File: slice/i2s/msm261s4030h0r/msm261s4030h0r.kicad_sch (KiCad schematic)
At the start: 3 parts, among them U1 MSM261S4030H0R

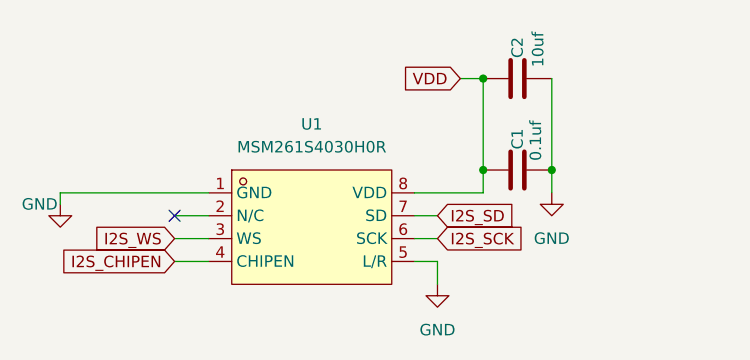
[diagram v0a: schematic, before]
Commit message: Update position of capacitor in `i2s/msm261s4030h0r`
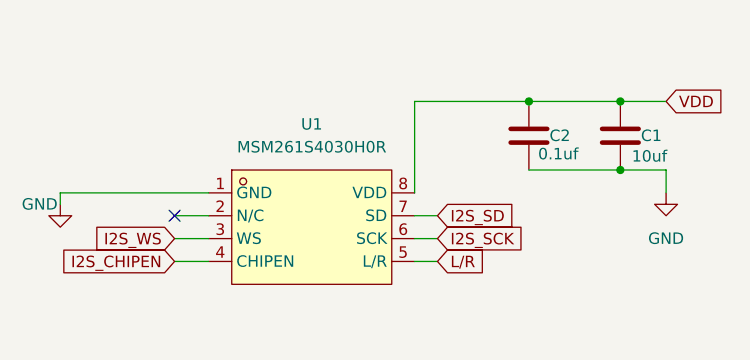
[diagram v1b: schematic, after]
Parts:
- C1: value 0.1uf -> 10uf
- C2: value 10uf -> 0.1uf
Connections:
- net GND: no longer U1.5 (L/R)
- new net L/R: U1.5 (L/R)
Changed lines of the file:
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@@
 	(paper "A4")
 	(junction
-		(at 175.26 92.71)
+		(at 182.88 85.09)
 		(diameter 0)
 		(color 0 0 0 0)
 	)
 	(junction
-		(at 167.64 82.55)
+		(at 172.72 85.09)
 		(diameter 0)
 		(color 0 0 0 0)
 	)
 	(junction
-		(at 167.64 92.71)
+		(at 182.88 92.71)
 		(diameter 0)
 		(color 0 0 0 0)
@@
 	(wire
 		(pts
-			(xy 167.64 92.71) (xy 167.64 95.25)
-		)
-		(stroke
-			(width 0)
-			(type default)
-		)
-	)
-	(wire
-		(pts
-			(xy 162.56 102.87) (xy 162.56 105.41)
-		)
-		(stroke
-			(width 0)
-			(type default)
-		)
-	)
-	(wire
-		(pts
-			(xy 175.26 92.71) (xy 175.26 95.25)
+			(xy 187.96 92.71) (xy 187.96 95.25)
+		)
+		(stroke
+			(width 0)
+			(type default)
+		)
+	)
+	(wire
+		(pts
+			(xy 172.72 85.09) (xy 182.88 85.09)
 		)
 		(stroke
@@
 	(wire
 		(pts
-			(xy 167.64 95.25) (xy 160.02 95.25)
+			(xy 172.72 92.71) (xy 182.88 92.71)
 		)
 		(stroke
@@
 	(wire
 		(pts
-			(xy 165.1 82.55) (xy 167.64 82.55)
-		)
-		(stroke
-			(width 0)
-			(type default)
-		)
-	)
-	(wire
-		(pts
-			(xy 167.64 82.55) (xy 167.64 92.71)
+			(xy 187.96 92.71) (xy 182.88 92.71)
 		)
 		(stroke
@@
 	(wire
 		(pts
+			(xy 160.02 85.09) (xy 160.02 95.25)
+		)
+		(stroke
+			(width 0)
+			(type default)
+		)
+	)
+	(wire
+		(pts
 			(xy 133.35 100.33) (xy 137.16 100.33)
 		)
@@
 	(wire
 		(pts
-			(xy 175.26 92.71) (xy 175.26 82.55)
+			(xy 160.02 85.09) (xy 172.72 85.09)
+		)
+		(stroke
+			(width 0)
+			(type default)
+		)
+	)
+	(wire
+		(pts
+			(xy 182.88 85.09) (xy 187.96 85.09)
 		)
 		(stroke
@@
 		)
 	)
+	(global_label "L{slash}R"
+		(shape input)
+		(at 162.56 102.87 0)
+		(fields_autoplaced yes)
+		(effects
+			(font
+				(size 1.27 1.27)
+			)
+			(justify left)
+		)
+		(property "Intersheetrefs" "${INTERSHEET_REFS}"
+			(at 169.1738 102.87 0)
+			(effects
+				(font
+					(size 1.27 1.27)
+				)
+				(justify left)
+				(hide yes)
+			)
+		)
+	)
 	(global_label "I2S_CHIPEN"
 		(shape input)
@@
 	(global_label "VDD"
 		(shape input)
-		(at 165.1 82.55 180)
+		(at 187.96 85.09 0)
 		(fields_autoplaced yes)
 		(effects
@@
 				(size 1.27 1.27)
 			)
-			(justify right)
+			(justify left)
 		)
 		(property "Intersheetrefs" "${INTERSHEET_REFS}"
-			(at 158.4862 82.55 0)
-			(effects
-				(font
-					(size 1.27 1.27)
-				)
-				(justify right)
+			(at 194.5738 85.09 0)
+			(effects
+				(font
+					(size 1.27 1.27)
+				)
+				(justify left)
 				(hide yes)
 			)
@@
 	(symbol
 		(lib_id "power:GND")
-		(at 175.26 95.25 0)
+		(at 187.96 95.25 0)
 		(unit 1)
 		(exclude_from_sim no)
@@
 		(dnp no)
 		(fields_autoplaced yes)
-		(property "Reference" "#PWR03"
-			(at 175.26 101.6 0)
+		(property "Reference" "#PWR01"
+			(at 187.96 101.6 0)
 			(effects
 				(font
@@
 		)
 		(property "Value" "GND"
-			(at 175.26 100.33 0)
+			(at 187.96 100.33 0)
 			(effects
 				(font
@@
 		)
 		(property "Footprint" ""
-			(at 175.26 95.25 0)
+			(at 187.96 95.25 0)
 			(effects
 				(font
@@
 		)
 		(property "Datasheet" ""
-			(at 175.26 95.25 0)
+			(at 187.96 95.25 0)
 			(effects
 				(font
@@
 		)
 		(property "Description" "Power symbol creates a global label with name \"GND\" , ground"
-			(at 175.26 95.25 0)
+			(at 187.96 95.25 0)
 			(effects
 				(font
@@
 		(instances
 			(project "msm261s4030h0r"
-				(path "/3ead2bbc-d546-4367-b51b-7ed83f32863a"
-					(reference "#PWR03")
-					(unit 1)
-				)
-			)
-		)
-	)
-	(symbol
-		(lib_id "Device:C")
-		(at 171.45 92.71 90)
-		(unit 1)
-		(exclude_from_sim no)
-		(in_bom yes)
-		(on_board yes)
-		(dnp no)
-		(property "Reference" "C1"
-			(at 171.45 90.424 0)
-			(do_not_autoplace yes)
-			(effects
-				(font
-					(size 1.27 1.27)
-				)
-				(justify left)
-			)
-		)
-		(property "Value" "0.1uf"
-			(at 173.482 91.694 0)
-			(do_not_autoplace yes)
-			(effects
-				(font
-					(size 1.27 1.27)
-				)
-				(justify left)
-			)
-		)
-		(property "Footprint" ""
-			(at 175.26 91.7448 0)
-			(effects
-				(font
-					(size 1.27 1.27)
-				)
-				(hide yes)
-			)
-		)
-		(property "Datasheet" "~"
-			(at 171.45 92.71 0)
-			(effects
-				(font
-					(size 1.27 1.27)
-				)
-				(hide yes)
-			)
-		)
-		(property "Description" "Unpolarized capacitor"
-			(at 171.45 92.71 0)
-			(effects
-				(font
-					(size 1.27 1.27)
-				)
-				(hide yes)
-			)
-		)
-		(pin "1"
-		)
-		(pin "2"
-		)
-		(instances
-			(project "msm261s4030h0r"
-				(path "/3ead2bbc-d546-4367-b51b-7ed83f32863a"
-					(reference "C1")
-					(unit 1)
-				)
-			)
-		)
-	)
-	(symbol
-		(lib_id "power:GND")
-		(at 162.56 105.41 0)
-		(unit 1)
-		(exclude_from_sim no)
-		(in_bom yes)
-		(on_board yes)
-		(dnp no)
-		(fields_autoplaced yes)
-		(property "Reference" "#PWR01"
-			(at 162.56 111.76 0)
-			(effects
-				(font
-					(size 1.27 1.27)
-				)
-				(hide yes)
-			)
-		)
-		(property "Value" "GND"
-			(at 162.56 110.49 0)
-			(effects
-				(font
-					(size 1.27 1.27)
-				)
-			)
-		)
-		(property "Footprint" ""
-			(at 162.56 105.41 0)
-			(effects
-				(font
-					(size 1.27 1.27)
-				)
-				(hide yes)
-			)
-		)
-		(property "Datasheet" ""
-			(at 162.56 105.41 0)
-			(effects
-				(font
-					(size 1.27 1.27)
-				)
-				(hide yes)
-			)
-		)
-		(property "Description" "Power symbol creates a global label with name \"GND\" , ground"
-			(at 162.56 105.41 0)
-			(effects
-				(font
-					(size 1.27 1.27)
-				)
-				(hide yes)
-			)
-		)
-		(pin "1"
-		)
-		(instances
-			(project ""
 				(path "/3ead2bbc-d546-4367-b51b-7ed83f32863a"
 					(reference "#PWR01")
@@
 	(symbol
 		(lib_id "Device:C")
-		(at 171.45 82.55 90)
+		(at 182.88 88.9 0)
+		(unit 1)
+		(exclude_from_sim no)
+		(in_bom yes)
+		(on_board yes)
+		(dnp no)
+		(property "Reference" "C1"
+			(at 185.166 88.9 0)
+			(do_not_autoplace yes)
+			(effects
+				(font
+					(size 1.27 1.27)
+				)
+				(justify left)
+			)
+		)
+		(property "Value" "10uf"
+			(at 184.15 91.186 0)
+			(do_not_autoplace yes)
+			(effects
+				(font
+					(size 1.27 1.27)
+				)
+				(justify left)
+			)
+		)
+		(property "Footprint" ""
+			(at 183.8452 92.71 0)
+			(effects
+				(font
+					(size 1.27 1.27)
+				)
+				(hide yes)
+			)
+		)
+		(property "Datasheet" "~"
+			(at 182.88 88.9 0)
+			(effects
+				(font
+					(size 1.27 1.27)
+				)
+				(hide yes)
+			)
+		)
+		(property "Description" "Unpolarized capacitor"
+			(at 182.88 88.9 0)
+			(effects
+				(font
+					(size 1.27 1.27)
+				)
+				(hide yes)
+			)
+		)
+		(pin "1"
+		)
+		(pin "2"
+		)
+		(instances
+			(project "msm261s4030h0r"
+				(path "/3ead2bbc-d546-4367-b51b-7ed83f32863a"
+					(reference "C1")
+					(unit 1)
+				)
+			)
+		)
+	)
+	(symbol
+		(lib_id "Device:C")
+		(at 172.72 88.9 0)
 		(unit 1)
 		(exclude_from_sim no)
@@
 		(dnp no)
 		(property "Reference" "C2"
-			(at 171.45 80.264 0)
+			(at 175.006 88.9 0)
 			(do_not_autoplace yes)
 			(effects
@@
 			)
 		)
-		(property "Value" "10uf"
-			(at 173.736 81.28 0)
+		(property "Value" "0.1uf"
+			(at 173.736 90.932 0)
 			(do_not_autoplace yes)
 			(effects
@@
 		)
 		(property "Footprint" ""
-			(at 175.26 81.5848 0)
+			(at 173.6852 92.71 0)
 			(effects
 				(font
@@
 		)
 		(property "Datasheet" "~"
-			(at 171.45 82.55 0)
+			(at 172.72 88.9 0)
 			(effects
 				(font
@@
 		)
 		(property "Description" "Unpolarized capacitor"
-			(at 171.45 82.55 0)
-			(effects
-				(font
+			(at 172.72 88.9 0)
+			(effects
+				(font
